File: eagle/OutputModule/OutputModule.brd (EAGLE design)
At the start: 74.9 x 54.4 mm, 30 parts, among them IC1 MCP23017SP

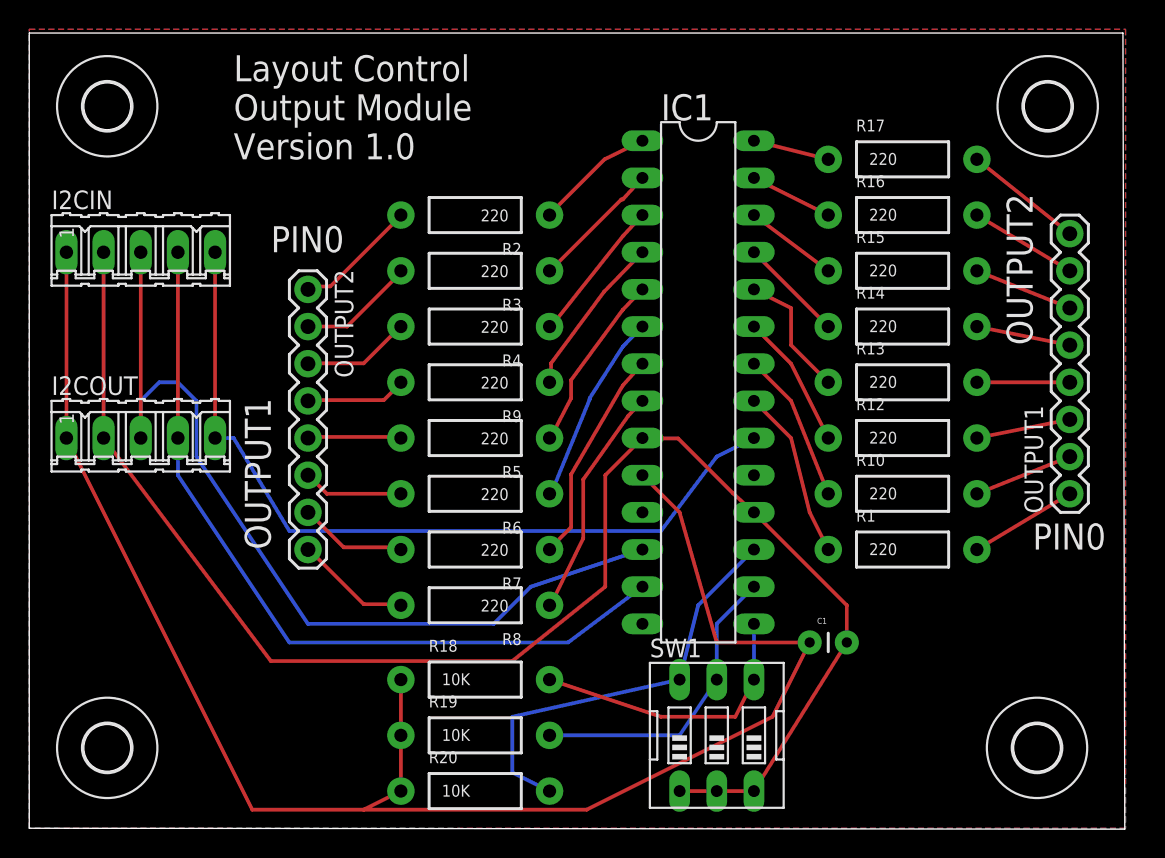
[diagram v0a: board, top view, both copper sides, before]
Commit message: 1.  Cleanup continues.  BlockController and the corresponding controller are deprecated along with SignalController and it's controller board.  These are replaced by the InputModule and OutputModule respectively 2.  TurnoutHandler moved to the MultiModuleController project folder 3.  Module moved to the MultiModuleController project folder 4.  More database cleanup work completed.
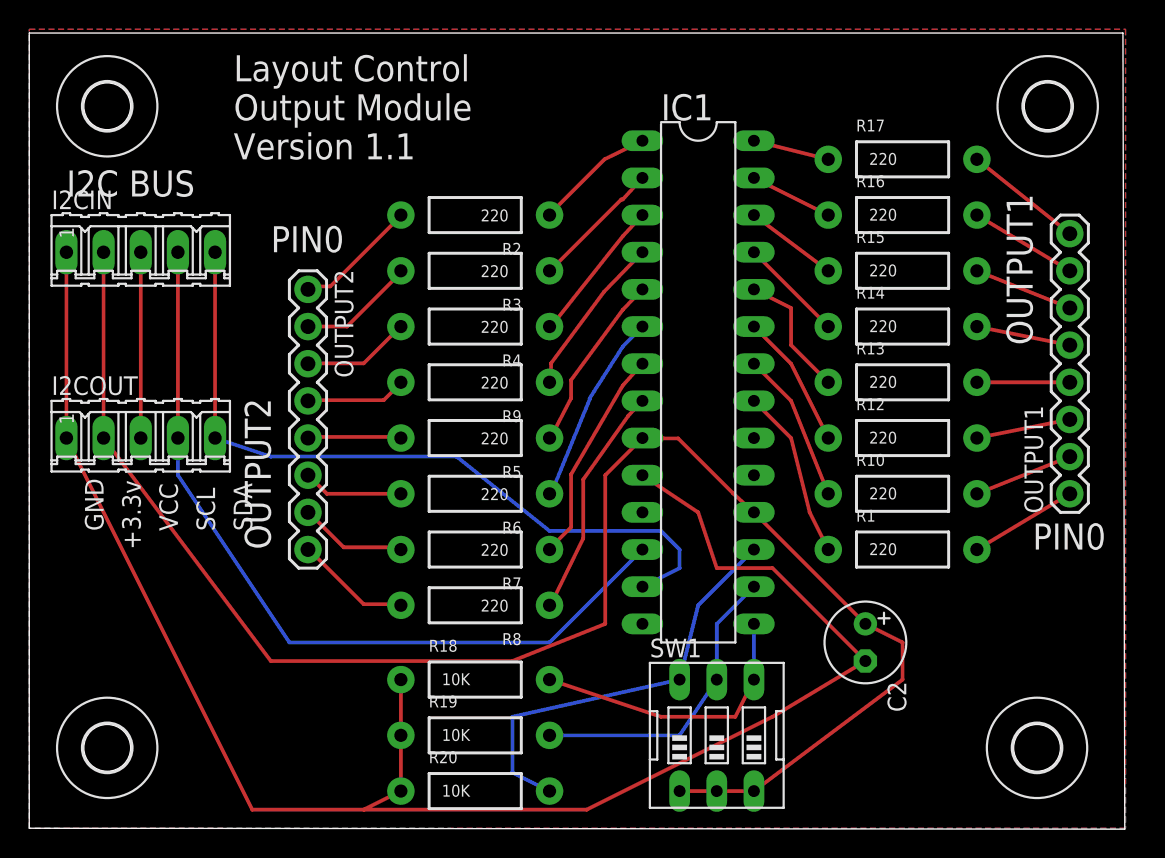
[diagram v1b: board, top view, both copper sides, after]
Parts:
- removed C1: (no value), SparkFun-Capacitors:CAP-PTH-SMALL
- added C2: 10uF, rcl:E2,5-6
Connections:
- removed net INT: I2CIN.5, I2COUT.5, IC1.20
- new net VCC: I2CIN.3, I2COUT.3
- net +3V3: now also C2.+; no longer C1.2
- net GND: now also C2.-; no longer C1.1
- net SCL: now also I2CIN.4, I2COUT.4; no longer I2CIN.3, I2COUT.3
- net SDA: now also I2CIN.5, I2COUT.5; no longer I2CIN.4, I2COUT.4
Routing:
- net INT: track 56.0 -> 0.00 mm
- net VCC: track 0.00 -> 14.0 mm
- net SCL: track 63.2 -> 55.7 mm
- net +3V3: track 105.9 -> 112.5 mm
- net GND: track 113.5 -> 117.4 mm
- net SDA: track 54.4 -> 51.1 mm
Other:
- board text added: "+3.3v"
- board text added: "GND"
- board text added: "I2C BUS"
- board text added: "Layout Control Output Module Version 1.1"
- board text added: "SCL"
- board text added: "SDA"
- board text added: "VCC"
- board text removed: "Layout Control Output Module Version 1.0"
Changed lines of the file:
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@@
 <text x="13.97" y="45.72" size="1.778" layer="21">Layout Control
 Output Module
-Version 1.0</text>
+Version 1.1</text>
 <text x="16.51" y="39.37" size="1.778" layer="21">PIN0</text>
 <text x="68.58" y="19.05" size="1.778" layer="21">PIN0</text>
-<text x="16.51" y="19.05" size="1.778" layer="21" rot="R90">OUTPUT1</text>
-<text x="68.58" y="33.02" size="1.778" layer="21" rot="R90">OUTPUT2</text>
+<text x="16.51" y="19.05" size="1.778" layer="21" rot="R90">OUTPUT2</text>
+<text x="68.58" y="33.02" size="1.778" layer="21" rot="R90">OUTPUT1</text>
+<text x="2.54" y="43.18" size="1.778" layer="21">I2C BUS</text>
+<text x="5.08" y="20.32" size="1.27" layer="21" rot="R90">GND
+</text>
+<text x="7.62" y="19.05" size="1.27" layer="21" rot="R90">+3.3v
+</text>
+<text x="10.16" y="20.32" size="1.27" layer="21" rot="R90">VCC
+</text>
+<text x="12.7" y="20.32" size="1.27" layer="21" rot="R90">SCL
+</text>
+<text x="15.24" y="20.32" size="1.27" layer="21" rot="R90">SDA
+</text>
 </plain>
 <attributes>
@@
 <attribute name="MF" value="" x="7.62" y="39.37" size="1.778" layer="27" display="off"/>
 </element>
-<element name="C1" library="SparkFun-Capacitors" package="CAP-PTH-SMALL" value="" x="53.34" y="12.7"/>
 <element name="SW1" library="special" package="EDG-03" value="" x="46.99" y="6.35"/>
 <element name="R18" library="SparkFun-Passives" package="AXIAL-0.4" value="10K" x="30.48" y="10.16"/>
 <element name="R19" library="SparkFun-Passives" package="AXIAL-0.4" value="10K" x="30.48" y="6.35"/>
 <element name="R20" library="SparkFun-Passives" package="AXIAL-0.4" value="10K" x="30.48" y="2.54"/>
+<element name="C2" library="rcl" package="E2,5-6" value="10uF" x="57.15" y="12.7" rot="R270"/>
 </elements>
 <signals>
-<signal name="SCL">
-<contactref element="IC1" pad="12"/>
+<signal name="VCC">
 <contactref element="I2COUT" pad="3"/>
 <contactref element="I2CIN" pad="3"/>
 <wire x1="7.62" y1="39.37" x2="7.62" y2="26.67" width="0.254" layer="1"/>
 <wire x1="7.62" y1="26.67" x2="7.62" y2="25.4" width="0.254" layer="16"/>
-<wire x1="41.91" y1="19.05" x2="34.29" y2="16.51" width="0.254" layer="16"/>
-<wire x1="34.29" y1="16.51" x2="31.75" y2="13.97" width="0.254" layer="16"/>
-<wire x1="31.75" y1="13.97" x2="19.05" y2="13.97" width="0.254" layer="16"/>
-<wire x1="19.05" y1="13.97" x2="11.43" y2="25.4" width="0.254" layer="16"/>
-<wire x1="11.43" y1="25.4" x2="11.43" y2="29.21" width="0.254" layer="16"/>
-<wire x1="11.43" y1="29.21" x2="10.16" y2="30.48" width="0.254" layer="16"/>
-<wire x1="10.16" y1="30.48" x2="8.89" y2="30.48" width="0.254" layer="16"/>
-<wire x1="8.89" y1="30.48" x2="7.62" y2="29.21" width="0.254" layer="16"/>
-<wire x1="7.62" y1="29.21" x2="7.62" y2="26.67" width="0.254" layer="16"/>
-</signal>
-<signal name="SDA">
-<contactref element="IC1" pad="13"/>
+</signal>
+<signal name="SCL">
 <contactref element="I2COUT" pad="4"/>
 <contactref element="I2CIN" pad="4"/>
@@
 <wire x1="10.16" y1="26.67" x2="10.16" y2="24.13" width="0.254" layer="16"/>
 <wire x1="10.16" y1="24.13" x2="17.78" y2="12.7" width="0.254" layer="16"/>
-<wire x1="17.78" y1="12.7" x2="36.83" y2="12.7" width="0.254" layer="16"/>
-<wire x1="36.83" y1="12.7" x2="41.91" y2="16.51" width="0.254" layer="16"/>
-</signal>
-<signal name="INT">
-<contactref element="IC1" pad="20"/>
+<wire x1="17.78" y1="12.7" x2="35.56" y2="12.7" width="0.254" layer="16"/>
+<contactref element="IC1" pad="12"/>
+<wire x1="35.56" y1="12.7" x2="41.91" y2="19.05" width="0.254" layer="16"/>
+</signal>
+<signal name="SDA">
 <contactref element="I2COUT" pad="5"/>
-<wire x1="12.7" y1="26.67" x2="13.97" y2="26.67" width="0.254" layer="16"/>
-<wire x1="13.97" y1="26.67" x2="17.78" y2="20.32" width="0.254" layer="16"/>
-<wire x1="17.78" y1="20.32" x2="43.18" y2="20.32" width="0.254" layer="16"/>
-<wire x1="43.18" y1="20.32" x2="46.99" y2="25.4" width="0.254" layer="16"/>
-<wire x1="46.99" y1="25.4" x2="49.53" y2="26.67" width="0.254" layer="16"/>
 <contactref element="I2CIN" pad="5"/>
 <wire x1="12.7" y1="39.37" x2="12.7" y2="26.67" width="0.254" layer="1"/>
+<contactref element="IC1" pad="13"/>
+<wire x1="12.7" y1="26.67" x2="16.51" y2="25.4" width="0.254" layer="16"/>
+<wire x1="16.51" y1="25.4" x2="29.21" y2="25.4" width="0.254" layer="16"/>
+<wire x1="29.21" y1="25.4" x2="35.56" y2="20.32" width="0.254" layer="16"/>
+<wire x1="35.56" y1="20.32" x2="43.18" y2="20.32" width="0.254" layer="16"/>
+<wire x1="43.18" y1="20.32" x2="44.45" y2="19.05" width="0.254" layer="16"/>
+<wire x1="44.45" y1="19.05" x2="44.45" y2="17.78" width="0.254" layer="16"/>
+<wire x1="44.45" y1="17.78" x2="41.91" y2="16.51" width="0.254" layer="16"/>
 </signal>
 <signal name="GND">
@@
 <contactref element="I2CIN" pad="1"/>
 <wire x1="2.54" y1="39.37" x2="2.54" y2="26.67" width="0.254" layer="1"/>
-<contactref element="C1" pad="1"/>
-<wire x1="53.34" y1="12.7" x2="46.99" y2="12.7" width="0.254" layer="1"/>
-<wire x1="46.99" y1="12.7" x2="44.45" y2="21.59" width="0.254" layer="1"/>
-<wire x1="44.45" y1="21.59" x2="41.91" y2="24.13" width="0.254" layer="1"/>
+<wire x1="45.72" y1="21.59" x2="41.91" y2="24.13" width="0.254" layer="1"/>
 <wire x1="2.54" y1="26.67" x2="15.24" y2="1.27" width="0.254" layer="1"/>
 <wire x1="15.24" y1="1.27" x2="22.86" y2="1.27" width="0.254" layer="1"/>
@@
 <wire x1="25.4" y1="2.54" x2="22.86" y2="1.27" width="0.254" layer="1"/>
 <wire x1="38.1" y1="1.27" x2="50.8" y2="7.62" width="0.254" layer="1"/>
-<wire x1="50.8" y1="7.62" x2="53.34" y2="12.7" width="0.254" layer="1"/>
 <polygon width="0.254" layer="16" isolate="0.3048">
 <vertex x="0" y="0"/>
@@
 <vertex x="74.93" y="0"/>
 </polygon>
+<contactref element="C2" pad="-"/>
+<wire x1="57.15" y1="11.43" x2="50.8" y2="7.62" width="0.254" layer="1"/>
+<wire x1="45.72" y1="21.59" x2="46.99" y2="17.78" width="0.254" layer="1"/>
+<wire x1="46.99" y1="17.78" x2="50.8" y2="17.78" width="0.254" layer="1"/>
+<wire x1="50.8" y1="17.78" x2="57.15" y2="11.43" width="0.254" layer="1"/>
 </signal>
 <signal name="ADD0">
@@
 <contactref element="I2CIN" pad="2"/>
 <wire x1="5.08" y1="39.37" x2="5.08" y2="26.67" width="0.254" layer="1"/>
-<contactref element="C1" pad="2"/>
 <wire x1="16.51" y1="11.43" x2="5.08" y2="26.67" width="0.254" layer="1"/>
-<wire x1="39.37" y1="16.51" x2="39.37" y2="24.13" width="0.254" layer="1"/>
+<wire x1="39.37" y1="13.97" x2="39.37" y2="24.13" width="0.254" layer="1"/>
 <wire x1="39.37" y1="24.13" x2="41.91" y2="26.67" width="0.254" layer="1"/>
-<wire x1="49.53" y1="21.59" x2="55.88" y2="15.24" width="0.254" layer="1"/>
-<wire x1="55.88" y1="15.24" x2="55.88" y2="12.7" width="0.254" layer="1"/>
+<wire x1="49.53" y1="21.59" x2="57.15" y2="13.97" width="0.254" layer="1"/>
 <contactref element="SW1" pad="3"/>
 <contactref element="SW1" pad="1"/>
@@
 <wire x1="46.99" y1="2.54" x2="44.45" y2="2.54" width="0.254" layer="1"/>
 <wire x1="16.51" y1="11.43" x2="33.02" y2="11.43" width="0.254" layer="1"/>
-<wire x1="33.02" y1="11.43" x2="39.37" y2="16.51" width="0.254" layer="1"/>
-<wire x1="49.53" y1="2.54" x2="55.88" y2="12.7" width="0.254" layer="1"/>
+<wire x1="33.02" y1="11.43" x2="39.37" y2="13.97" width="0.254" layer="1"/>
+<contactref element="C2" pad="+"/>
+<wire x1="49.53" y1="2.54" x2="59.69" y2="10.16" width="0.254" layer="1"/>
+<wire x1="59.69" y1="10.16" x2="59.69" y2="12.7" width="0.254" layer="1"/>
+<wire x1="59.69" y1="12.7" x2="57.15" y2="13.97" width="0.254" layer="1"/>
 </signal>
 <signal name="N$7">

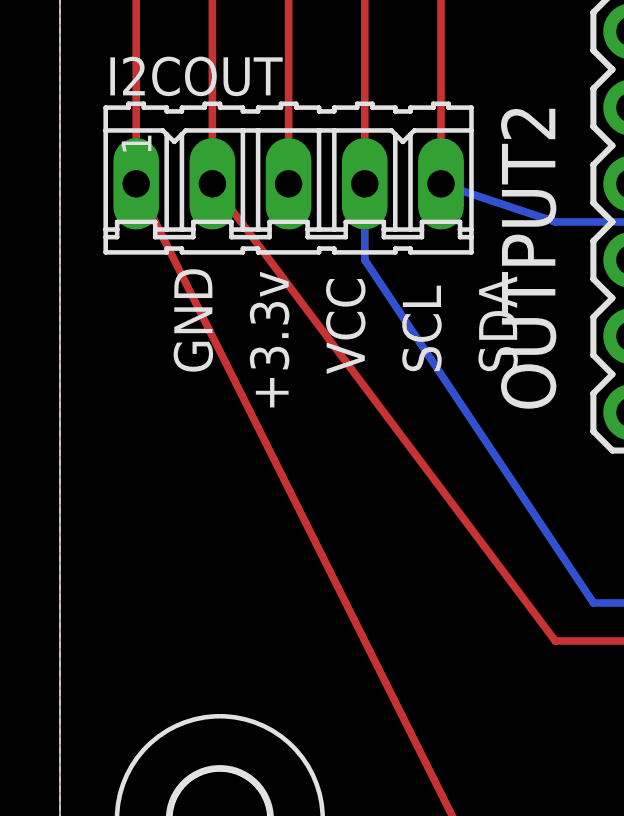
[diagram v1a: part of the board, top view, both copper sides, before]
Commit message: 1.  Cleanup work 2.  Reduced the retry timeout to 2 seconds (from 3) 3.  Change the TurnoutModule board to use the same address pins as the other modules 4.  Add a two-pin header to Input and Output module boards with access to GND and 3.3v 5.  Move the call to module->finishxxx to before network setup code so that the modules can initialize while the network connection is being established
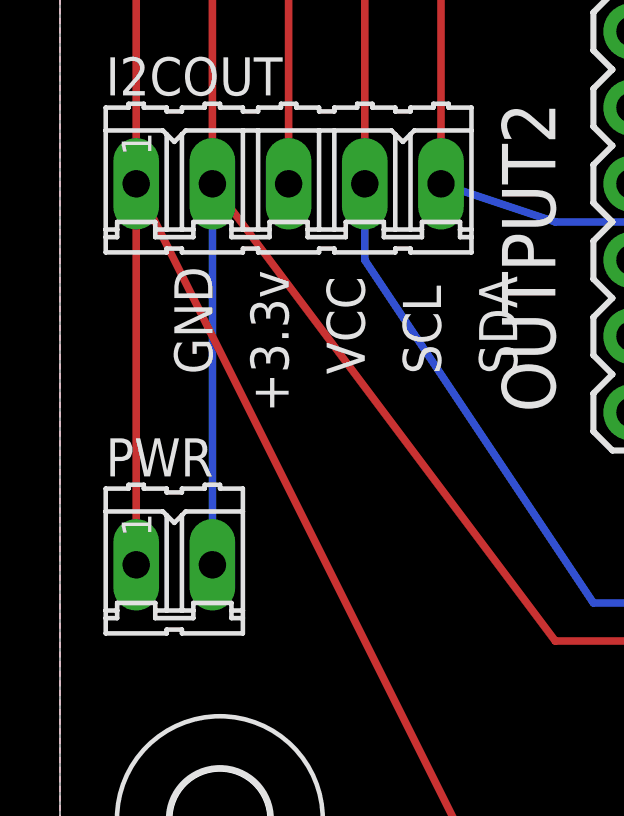
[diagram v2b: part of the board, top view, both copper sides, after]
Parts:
- added PWR: PIN0, con-amp-quick:02P
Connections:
- net +3V3: now also PWR.2
- net GND: now also PWR.1
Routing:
- net GND: track 117.4 -> 130.1 mm
- net +3V3: track 112.5 -> 125.2 mm
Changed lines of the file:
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@@
 <element name="R20" library="SparkFun-Passives" package="AXIAL-0.4" value="10K" x="30.48" y="2.54"/>
 <element name="C2" library="rcl" package="E2,5-6" value="10uF" x="57.15" y="12.7" rot="R270"/>
+<element name="PWR" library="con-amp-quick" package="02P" value="PIN0" x="3.81" y="13.97">
+<attribute name="MF" value="" x="3.81" y="13.97" size="1.778" layer="27" display="off"/>
+<attribute name="OC_NEWARK" value="unknown" x="3.81" y="13.97" size="1.778" layer="27" display="off"/>
+<attribute name="MPN" value="" x="3.81" y="13.97" size="1.778" layer="27" display="off"/>
+<attribute name="OC_FARNELL" value="unknown" x="3.81" y="13.97" size="1.778" layer="27" display="off"/>
+</element>
 </elements>
 <signals>
@@
 <wire x1="46.99" y1="17.78" x2="50.8" y2="17.78" width="0.254" layer="1"/>
 <wire x1="50.8" y1="17.78" x2="57.15" y2="11.43" width="0.254" layer="1"/>
+<contactref element="PWR" pad="1"/>
+<wire x1="2.54" y1="13.97" x2="2.54" y2="26.67" width="0.254" layer="1"/>
 </signal>
 <signal name="ADD0">
@@
 <wire x1="59.69" y1="10.16" x2="59.69" y2="12.7" width="0.254" layer="1"/>
 <wire x1="59.69" y1="12.7" x2="57.15" y2="13.97" width="0.254" layer="1"/>
+<contactref element="PWR" pad="2"/>
+<wire x1="5.08" y1="13.97" x2="5.08" y2="26.67" width="0.254" layer="16"/>
 </signal>
 <signal name="N$7">
